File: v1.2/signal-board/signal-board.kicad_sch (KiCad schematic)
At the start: 45 parts, among them IC1 74HCT245, J1 Jack-DC, J2 Conn_01x12, J3 JST SM, J4 Conn_01x16, J5 switch_jumpers, J6 switch_jumpers, SW1 SW_MEC_5G, SW2 SW_MEC_5G, U1 TPS63060, U2 ESP32-DEVKITC-32D

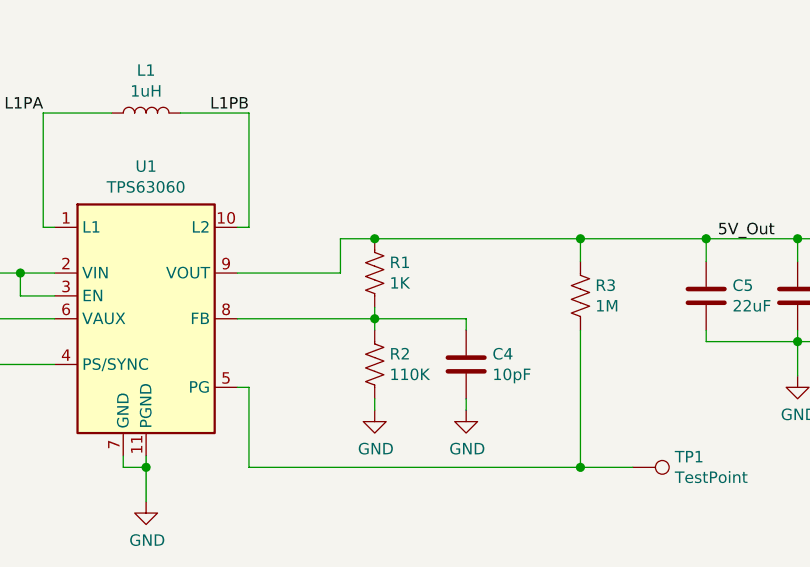
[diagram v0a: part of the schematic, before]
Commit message: added holes to corners
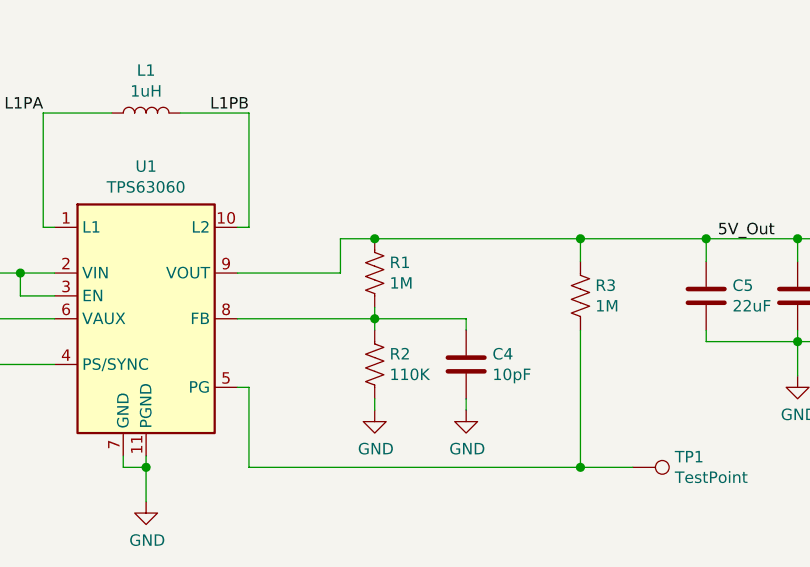
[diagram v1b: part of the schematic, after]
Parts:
- R1: value 1K -> 1M; LCSC C11702 -> C26083
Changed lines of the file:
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@@
-(kicad_sch (version 20200828) (generator eeschema)
+(kicad_sch (version 20201015) (generator eeschema)
   (page 1 1)
   (paper "A3")
@@
   (junction (at 275.59 229.87) (diameter 1.016) (color 0 0 0 0))
   (junction (at 285.75 218.44) (diameter 1.016) (color 0 0 0 0))
+  (no_connect (at 181.61 48.26))
+  (no_connect (at 181.61 76.2))
+  (no_connect (at 222.25 76.2))
+  (no_connect (at 181.61 73.66))
+  (no_connect (at 181.61 71.12))
   (no_connect (at 222.25 78.74))
   (no_connect (at 181.61 50.8))
-  (no_connect (at 181.61 71.12))
-  (no_connect (at 181.61 48.26))
-  (no_connect (at 181.61 76.2))
-  (no_connect (at 181.61 73.66))
   (no_connect (at 222.25 73.66))
-  (no_connect (at 222.25 76.2))
   (wire (pts (xy 36.83 187.96) (xy 46.99 187.96))
     (stroke (width 0) (type solid) (color 0 0 0 0))
@@
       (effects (font (size 1.27 1.27)) (justify left))
     )
-    (property "Value" "1K" (id 1) (at 230.251 223.393 0)
+    (property "Value" "1M" (id 1) (at 230.251 223.393 0)
       (effects (font (size 1.27 1.27)) (justify left))
     )
@@
       (effects (font (size 1.27 1.27)) hide)
     )
-    (property "LCSC" "C11702" (id 5) (at 228.6 222.25 0)
+    (property "LCSC" "C26083" (id 5) (at 228.6 222.25 0)
       (effects (font (size 1.27 1.27)) hide)
     )
@@
     )
   )
+  (sheet_instances
+    (path "/" (page "1"))
+  )
   (symbol_instances
     (path "/00000000-0000-0000-0000-00005f29365f"
@@
     )
     (path "/00000000-0000-0000-0000-00005ed5e669"
-      (reference "R1") (unit 1) (value "1K") (footprint "Resistor_SMD:R_0402_1005Metric")
+      (reference "R1") (unit 1) (value "1M") (footprint "Resistor_SMD:R_0402_1005Metric")
     )
     (path "/00000000-0000-0000-0000-00005ed5e8ca"

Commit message: updated symbol and footprint links
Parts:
- IC1: footprint 74HCT245:SOIC-20W_7.5x10.0mm_P1.27mm -> GlowFlock footprints:SOIC-20W_7.5x10.0mm_P1.27mm
- J1: DigiKey100 1.03 -> 0.53; DigiKeyPN CP-063AH-ND -> CP-002AH-ND; Supplier Part PJ-063AH -> PJ-002AH
- SW1, SW2: footprint PTS 647:PTS647SK38SMTR2LFS -> GlowFlock footprints:PTS647SK38SMTR2LFS
- U2: footprint MODULE_ESP32-DEVKITC-32D -> GlowFlock footprints:MODULE_ESP32-DEVKITC-32D
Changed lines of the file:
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@@
   (junction (at 285.75 218.44) (diameter 1.016) (color 0 0 0 0))
   (no_connect (at 181.61 48.26))
+  (no_connect (at 181.61 50.8))
+  (no_connect (at 222.25 78.74))
+  (no_connect (at 181.61 71.12))
   (no_connect (at 181.61 76.2))
+  (no_connect (at 222.25 73.66))
+  (no_connect (at 181.61 73.66))
   (no_connect (at 222.25 76.2))
-  (no_connect (at 181.61 73.66))
-  (no_connect (at 181.61 71.12))
-  (no_connect (at 222.25 78.74))
-  (no_connect (at 181.61 50.8))
-  (no_connect (at 222.25 73.66))
   (wire (pts (xy 36.83 187.96) (xy 46.99 187.96))
     (stroke (width 0) (type solid) (color 0 0 0 0))
@@
       (effects (font (size 1.27 1.27)) hide)
     )
-    (property "Footprint" "PTS 647:PTS647SK38SMTR2LFS" (id 2) (at 67.945 29.21 0)
+    (property "Footprint" "GlowFlock footprints:PTS647SK38SMTR2LFS" (id 2) (at 67.945 29.21 0)
       (effects (font (size 1.27 1.27)) hide)
     )
@@
       (effects (font (size 1.27 1.27)) hide)
     )
-    (property "Footprint" "PTS 647:PTS647SK38SMTR2LFS" (id 2) (at 67.945 63.5 0)
+    (property "Footprint" "GlowFlock footprints:PTS647SK38SMTR2LFS" (id 2) (at 67.945 63.5 0)
       (effects (font (size 1.27 1.27)) hide)
     )
@@
       (effects (font (size 1.27 1.27)) hide)
     )
-    (property "Supplier Part" "PJ-063AH" (id 4) (at 78.105 226.695 0)
-      (effects (font (size 1.27 1.27)) hide)
-    )
-    (property "DigiKey100" "1.03" (id 5) (at 78.105 226.695 0)
-      (effects (font (size 1.27 1.27)) hide)
-    )
-    (property "DigiKeyPN" "CP-063AH-ND" (id 6) (at 78.105 226.695 0)
+    (property "Supplier Part" "PJ-002AH" (id 4) (at 78.105 226.695 0)
+      (effects (font (size 1.27 1.27)) hide)
+    )
+    (property "DigiKey100" "0.53" (id 5) (at 78.105 226.695 0)
+      (effects (font (size 1.27 1.27)) hide)
+    )
+    (property "DigiKeyPN" "CP-002AH-ND" (id 6) (at 78.105 226.695 0)
       (effects (font (size 1.27 1.27)) hide)
     )
@@
     (property "Reference" "IC1" (id 0) (at 196.85 161.1376 0))
     (property "Value" "74HCT245" (id 1) (at 196.85 158.8262 0))
-    (property "Footprint" "74HCT245:SOIC-20W_7.5x10.0mm_P1.27mm" (id 2) (at 196.85 141.605 0)
+    (property "Footprint" "GlowFlock footprints:SOIC-20W_7.5x10.0mm_P1.27mm" (id 2) (at 196.85 141.605 0)
       (effects (font (size 1.27 1.27)) hide)
     )
@@
     (property "Reference" "U2" (id 0) (at 201.93 85.4964 0))
     (property "Value" "ESP32-DEVKITC-32D" (id 1) (at 201.93 83.185 0))
-    (property "Footprint" "MODULE_ESP32-DEVKITC-32D" (id 2) (at 201.93 55.88 0)
+    (property "Footprint" "GlowFlock footprints:MODULE_ESP32-DEVKITC-32D" (id 2) (at 201.93 55.88 0)
       (effects (font (size 1.27 1.27)) (justify left bottom) hide)
     )
@@
     )
     (path "/00000000-0000-0000-0000-00005e984fa4"
-      (reference "IC1") (unit 1) (value "74HCT245") (footprint "74HCT245:SOIC-20W_7.5x10.0mm_P1.27mm")
+      (reference "IC1") (unit 1) (value "74HCT245") (footprint "GlowFlock footprints:SOIC-20W_7.5x10.0mm_P1.27mm")
     )
     (path "/00000000-0000-0000-0000-00005f1fa557"
@@
     )
     (path "/00000000-0000-0000-0000-00005e8eb38f"
-      (reference "SW1") (unit 1) (value "SW_MEC_5G") (footprint "PTS 647:PTS647SK38SMTR2LFS")
+      (reference "SW1") (unit 1) (value "SW_MEC_5G") (footprint "GlowFlock footprints:PTS647SK38SMTR2LFS")
     )
     (path "/00000000-0000-0000-0000-00005e909fe3"
-      (reference "SW2") (unit 1) (value "SW_MEC_5G") (footprint "PTS 647:PTS647SK38SMTR2LFS")
+      (reference "SW2") (unit 1) (value "SW_MEC_5G") (footprint "GlowFlock footprints:PTS647SK38SMTR2LFS")
     )
     (path "/00000000-0000-0000-0000-00005f6fffd0"
@@
     )
     (path "/00000000-0000-0000-0000-00005e9027ab"
-      (reference "U2") (unit 1) (value "ESP32-DEVKITC-32D") (footprint "MODULE_ESP32-DEVKITC-32D")
-    )
-  )
+      (reference "U2") (unit 1) (value "ESP32-DEVKITC-32D") (footprint "GlowFlock footprints:MODULE_ESP32-DEVKITC-32D")
+    )
+  )

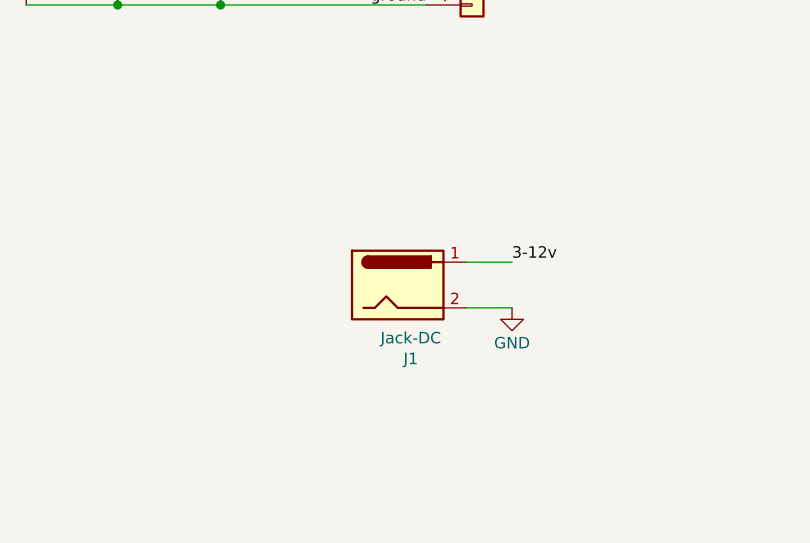
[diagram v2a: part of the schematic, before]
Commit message: got rid of footprints, added new dc jack
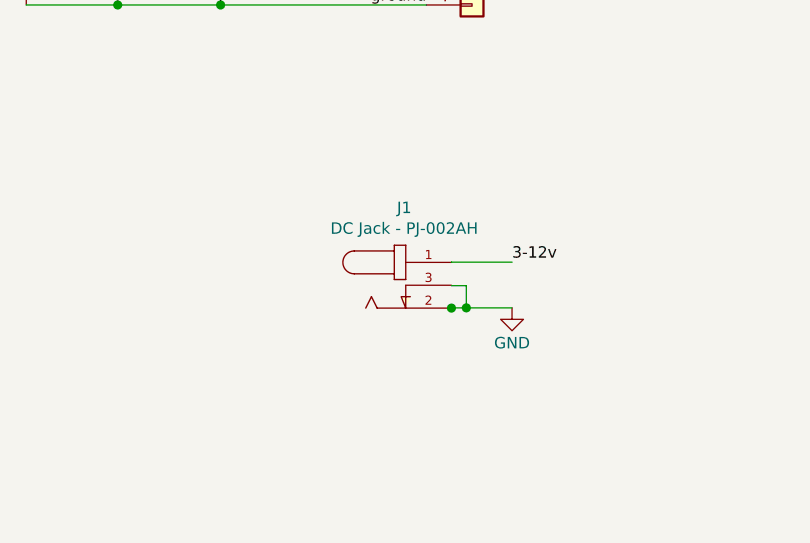
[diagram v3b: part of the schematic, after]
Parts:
- removed J1: Jack-DC, Connector_BarrelJack:BarrelJack_CUI_PJ-063AH_Horizontal, symbol Connector:Jack-DC
- added J1: DC Jack - PJ-002AH, GlowFlock footprints:CUI_PJ-002AH, symbol glowflock-dc-plug:PJ-002AH
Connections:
- net 3-12v: now also J1.1
- net GND: now also J1.2
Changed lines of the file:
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@@
   (junction (at 83.185 34.29) (diameter 1.016) (color 0 0 0 0))
   (junction (at 83.185 68.58) (diameter 1.016) (color 0 0 0 0))
+  (junction (at 84.074 229.2604) (diameter 1.016) (color 0 0 0 0))
+  (junction (at 85.725 229.235) (diameter 1.016) (color 0 0 0 0))
   (junction (at 149.86 222.25) (diameter 1.016) (color 0 0 0 0))
   (junction (at 158.75 222.25) (diameter 1.016) (color 0 0 0 0))
@@
   (no_connect (at 181.61 48.26))
   (no_connect (at 181.61 50.8))
+  (no_connect (at 222.25 73.66))
+  (no_connect (at 181.61 71.12))
+  (no_connect (at 181.61 73.66))
   (no_connect (at 222.25 78.74))
-  (no_connect (at 181.61 71.12))
+  (no_connect (at 222.25 76.2))
   (no_connect (at 181.61 76.2))
-  (no_connect (at 222.25 73.66))
-  (no_connect (at 181.61 73.66))
-  (no_connect (at 222.25 76.2))
   (wire (pts (xy 36.83 187.96) (xy 46.99 187.96))
     (stroke (width 0) (type solid) (color 0 0 0 0))
@@
     (stroke (width 0) (type solid) (color 0 0 0 0))
   )
-  (wire (pts (xy 85.725 224.155) (xy 90.805 224.155))
+  (wire (pts (xy 84.074 224.155) (xy 84.074 224.1804))
+    (stroke (width 0) (type solid) (color 0 0 0 0))
+  )
+  (wire (pts (xy 84.074 224.155) (xy 90.805 224.155))
+    (stroke (width 0) (type solid) (color 0 0 0 0))
+  )
+  (wire (pts (xy 84.074 226.7712) (xy 85.725 226.7712))
+    (stroke (width 0) (type solid) (color 0 0 0 0))
+  )
+  (wire (pts (xy 84.074 229.235) (xy 85.725 229.235))
+    (stroke (width 0) (type solid) (color 0 0 0 0))
+  )
+  (wire (pts (xy 84.074 229.2604) (xy 84.074 229.235))
+    (stroke (width 0) (type solid) (color 0 0 0 0))
+  )
+  (wire (pts (xy 84.074 229.3112) (xy 84.074 229.2604))
+    (stroke (width 0) (type solid) (color 0 0 0 0))
+  )
+  (wire (pts (xy 85.725 226.7712) (xy 85.725 229.235))
     (stroke (width 0) (type solid) (color 0 0 0 0))
   )
@@
     )
   )
-  (symbol (lib_id "Connector:Jack-DC") (at 78.105 226.695 0) (unit 1)
-    (in_bom yes) (on_board yes)
-    (property "Reference" "J1" (id 0) (at 79.5528 234.8992 0))
-    (property "Value" "Jack-DC" (id 1) (at 79.5528 232.5878 0))
-    (property "Footprint" "Connector_BarrelJack:BarrelJack_CUI_PJ-063AH_Horizontal" (id 2) (at 79.375 227.711 0)
-      (effects (font (size 1.27 1.27)) hide)
-    )
-    (property "Datasheet" "~" (id 3) (at 79.375 227.711 0)
-      (effects (font (size 1.27 1.27)) hide)
-    )
-    (property "Supplier Part" "PJ-002AH" (id 4) (at 78.105 226.695 0)
-      (effects (font (size 1.27 1.27)) hide)
-    )
-    (property "DigiKey100" "0.53" (id 5) (at 78.105 226.695 0)
-      (effects (font (size 1.27 1.27)) hide)
-    )
-    (property "DigiKeyPN" "CP-002AH-ND" (id 6) (at 78.105 226.695 0)
-      (effects (font (size 1.27 1.27)) hide)
+  (symbol (lib_id "glowflock-dc-plug:PJ-002AH") (at 78.994 226.7204 0) (unit 1)
+    (in_bom yes) (on_board yes)
+    (property "Reference" "J1" (id 0) (at 78.829 218.1158 0))
+    (property "Value" "DC Jack - PJ-002AH" (id 1) (at 78.829 220.4148 0))
+    (property "Footprint" "GlowFlock footprints:CUI_PJ-002AH" (id 2) (at 78.994 226.7204 0)
+      (effects (font (size 1.27 1.27)) (justify left bottom) hide)
+    )
+    (property "Datasheet" "" (id 3) (at 78.994 226.7204 0)
+      (effects (font (size 1.27 1.27)) (justify left bottom) hide)
+    )
+    (property "STANDARD" "Manufacturer recommendations" (id 4) (at 78.994 226.7204 0)
+      (effects (font (size 1.27 1.27)) (justify left bottom) hide)
+    )
+    (property "MANUFACTURER" "CUI INC" (id 5) (at 78.994 226.7204 0)
+      (effects (font (size 1.27 1.27)) (justify left bottom) hide)
     )
   )
@@
       (reference "IC1") (unit 1) (value "74HCT245") (footprint "GlowFlock footprints:SOIC-20W_7.5x10.0mm_P1.27mm")
     )
-    (path "/00000000-0000-0000-0000-00005f1fa557"
-      (reference "J1") (unit 1) (value "Jack-DC") (footprint "Connector_BarrelJack:BarrelJack_CUI_PJ-063AH_Horizontal")
+    (path "/43d93f35-2a7e-4c59-80e6-55bea576b4a8"
+      (reference "J1") (unit 1) (value "DC Jack - PJ-002AH") (footprint "GlowFlock footprints:CUI_PJ-002AH")
     )
     (path "/00000000-0000-0000-0000-00005f4f1eda"

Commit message: cleanup, new plug
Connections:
- net GND: no longer J1.2
- net at J1.3: now also J1.2
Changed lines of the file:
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@@
   (junction (at 83.185 68.58) (diameter 1.016) (color 0 0 0 0))
   (junction (at 84.074 229.2604) (diameter 1.016) (color 0 0 0 0))
-  (junction (at 85.725 229.235) (diameter 1.016) (color 0 0 0 0))
   (junction (at 149.86 222.25) (diameter 1.016) (color 0 0 0 0))
   (junction (at 158.75 222.25) (diameter 1.016) (color 0 0 0 0))
@@
   (junction (at 275.59 229.87) (diameter 1.016) (color 0 0 0 0))
   (junction (at 285.75 218.44) (diameter 1.016) (color 0 0 0 0))
-  (no_connect (at 181.61 48.26))
-  (no_connect (at 181.61 50.8))
   (no_connect (at 222.25 73.66))
   (no_connect (at 181.61 71.12))
+  (no_connect (at 222.25 76.2))
+  (no_connect (at 181.61 48.26))
+  (no_connect (at 181.61 76.2))
   (no_connect (at 181.61 73.66))
+  (no_connect (at 181.61 50.8))
   (no_connect (at 222.25 78.74))
-  (no_connect (at 222.25 76.2))
-  (no_connect (at 181.61 76.2))
   (wire (pts (xy 36.83 187.96) (xy 46.99 187.96))
     (stroke (width 0) (type solid) (color 0 0 0 0))
@@
     (stroke (width 0) (type solid) (color 0 0 0 0))
   )
-  (wire (pts (xy 84.074 226.7712) (xy 85.725 226.7712))
+  (wire (pts (xy 84.074 226.7204) (xy 84.074 229.2604))
     (stroke (width 0) (type solid) (color 0 0 0 0))
   )
-  (wire (pts (xy 84.074 229.235) (xy 85.725 229.235))
-    (stroke (width 0) (type solid) (color 0 0 0 0))
-  )
-  (wire (pts (xy 84.074 229.2604) (xy 84.074 229.235))
+  (wire (pts (xy 84.074 229.235) (xy 90.805 229.235))
     (stroke (width 0) (type solid) (color 0 0 0 0))
   )
@@
     (stroke (width 0) (type solid) (color 0 0 0 0))
   )
-  (wire (pts (xy 85.725 226.7712) (xy 85.725 229.235))
-    (stroke (width 0) (type solid) (color 0 0 0 0))
-  )
-  (wire (pts (xy 85.725 229.235) (xy 90.805 229.235))
-    (stroke (width 0) (type solid) (color 0 0 0 0))
-  )

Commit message: updates for v1.2
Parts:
- added 5V_SW1, TP1, TP10, TP11, TP2, TP2-3, TP3, TP4, TP6, TP8, TP9, TP_GND1, TP_GND2, TP_GND3, TP_GND4, TP_GND5, TP_GND6, TP_GND7, TP_GND8: TestPoint, TestPoint:TestPoint_Pad_D1.0mm, symbol Connector:TestPoint
- added C14: 10uF, Capacitor_SMD:C_0805_2012Metric_Pad1.15x1.40mm_HandSolder, symbol Device:C
- added C15: 100pF, Capacitor_SMD:C_0805_2012Metric_Pad1.15x1.40mm_HandSolder, symbol Device:C
- added C16, C17: 22uF, Capacitor_SMD:C_0805_2012Metric_Pad1.15x1.40mm_HandSolder, symbol Device:C
- added D3, D4: D, Diode_SMD:D_0603_1608Metric, symbol Device:D
- added F1: 3A Fuse, Fuse:Fuse_1206_3216Metric, symbol Device:Polyfuse
- added R18, R23: 0, Resistor_SMD:R_0402_1005Metric, symbol Device:R_US
- added R19: 4.7k, Resistor_SMD:R_0402_1005Metric, symbol Device:R_Small_US
- added R20, R21: 300K, Resistor_SMD:R_0402_1005Metric, symbol Device:R_US
- added R22: 15, Resistor_SMD:R_0402_1005Metric, symbol Device:R_US
- added R24: NP, Resistor_SMD:R_0402_1005Metric, symbol Device:R_US
- added U3: TPS2553DBVR, Package_TO_SOT_SMD:SOT-23-6_Handsoldering, symbol TPS2553DVBR:TPS2553DBVR
- added U4: TPS22810DBVR, Package_TO_SOT_SMD:SOT-23-6_Handsoldering, symbol TPS22810:TPS22810DBVR
- added U5: 74LVC1G32, Package_TO_SOT_SMD:SOT-353_SC-70-5_Handsoldering, symbol 74xGxx:74LVC1G32
- R1: value 1M -> 300K; LCSC C26083 -> C25774
- R2: value 110K -> 100K; LCSC C25745 -> C25741
- renumbered TP1 to TP5
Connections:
- net +5V: now also 5V_SW1.1, U3.6 (OUT); no longer C5.1, C6.1, C7.1, R1.1, R3.1, U1.9 (VOUT)
- net GND: now also J1.2, J1.3, C14.2, C15.2, C16.2, C17.2, D3.2 (A), D4.2 (A), R22.2, R24.1, TP2.1, TP4.1, TP_GND1.1, TP_GND2.1, TP_GND3.1, TP_GND4.1, TP_GND5.1, TP_GND6.1, TP_GND7.1, TP_GND8.1, U3.2 (GND), U4.2 (GND), U5.3 (GND)
- net L1PA: now also TP1.1
- net L1PB: now also TP10.1
- net pixels_1: now also D4.1 (K)
- net pixels_2: now also D3.1 (K)
- net 5V_Out_PG: now reaches R3.2, TP5.1, U1.5 (PG)
- net 5V_Out_PG: now also R23.1, U5.1
- net at C3.1, U1.6 (VAUX): now also TP6.1
- net TPS_FEEDBACK: now reaches C4.1, R2.1, U1.8 (FB)
- net TPS_FEEDBACK: now also R1.1, TP8.1; no longer R1.2
- net 3-12v renamed 3-12V_UNFUSED
- net 3-12V_UNFUSED: now also F1.1; no longer C1.1, C2.1, U1.2 (VIN), U1.3 (EN)
- new net: R1.2, R20.1
- new net: C16.1, C17.1, R19.2, TP3.1, U4.3 (EN/UVLO)
- new net: TP11.1, U3.4 (~FAULT~)
- new net: C15.1, U4.4 (CT)
- new net: R18.2, U4.5 (QOD)
- new net: R22.1, U3.5 (ILIM)
- new net: R20.2, R21.1
- new net 3-12V_FUSED: C14.1, F1.2, R19.1, U4.1 (VIN)
- new net 3-12V_FUSED_SW: C1.1, C2.1, R18.1, TP2-3.1, U1.2 (VIN), U1.3 (EN), U4.6 (VOUT)
- new net EN_2553: R23.2, R24.2, U3.3 (EN), U5.2, U5.4
- new net VCC: C5.1, C6.1, C7.1, R21.2, R3.1, TP9.1, U1.9 (VOUT), U3.1 (IN), U5.5 (VCC)
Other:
- note added: "15 ohm= 1.6A current limit"
- note added: "Buck-boost, outputs 5.0V from wide range input. Need to wait until output stabelizes before applying load. Need to limit inrush current or operation is unstable."
- note added: "CT limits inrush current to a configurable level. Quick discharge is optional. 100pf at 5v measured as a 10ms rise time."
- note added: "Delay EN by 50ms-100ms to allow current to inrush to attached LED strips."
- note added: "ESD Protection Diodes"
- note added: "NP, Optional Latch Output"
- note added: "U3: Only output power after TPS output has stabelized. Takes 10's of ms"
- moved on the sheet: C5, C6, C7, J1, R1, R2, R3, TP5
